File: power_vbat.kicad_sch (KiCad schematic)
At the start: 8 parts, among them J3 ESC pads (CURR TX M4 M3 M2 M1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

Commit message: updoot
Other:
- note added: "BOARD INPUTS: regulated 5 V at J3 pin 7 from an external converter, plus USB VBUS at J4. External choices: 2S-6S -> 5 V / 3 A buck, or 1S 18650 -> 5 V boost. J3 pin 9 carries raw battery voltage only to the R27/R28 sense divider. 5V_IN supplies servo power (J7 rows 7-10) and Q1. GPS/ELRS use V3V3_SYS."
- note added: "ESC PAD ROW J3: CURR, TX, M4, M3, M2, M1, 5V_IN, GND, VBAT. CURR -> R53/C78 -> GPIO42 (ADC2); TX -> R54 -> GPIO32 (PIO UART RX). Motor PWM4/3/2/1 -> GPIO36/38/39/43. Pin 7 receives regulated 5 V from an external buck or boost; C19 is its bulk capacitor. Pin 9 senses raw battery through R27/R28/C48 to GPIO41 (ADC1); it powers no load. Pad pitch is assumed 2.00 mm: confirm against the physical ESC.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"
- note removed: "BOARD INPUTS: REGULATED 5 V FROM AN EXTERNAL BEC on the ESC pad row J3 pin 7 (5V_IN), and USB VBUS ~5 V (J4). There is no on-board pack buck any more (DESIGN_SPEC "Decisions", 2026-09-17): raw pack reaches this board only as the J3 pin 9 SENSE wire VBAT, which drives the R27/R28/C48 divider and nothing else - no load, no bulk, no copper zone. 5V_IN is the servo / GPS / ELRS bus (IO block rows 1-4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"
- note removed: "ESC PAD ROW J3 (MicoAir AM32 4-in-1 ESC, FC-connection row), NINE PADS. Pads 1-6 are the ESC silkscreen read left to right; pads 7-9 are this board's power entry, added when the on-board pack buck was removed: 1 CURR - analog current sense from the ESC, 12.75 mV/A, 0-3.3 V -> R53/C78 -> GPIO42 (ADC2) on BOARD 1. 2 TX - KISS ESC telemetry, 3.3 V, 115200 baud, ESC output only -> R54 -> GPIO32 (PIO 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"

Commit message: update
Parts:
- C48: value 100n / 16 V X7R, ADC1 -> 100n / 16 V X7R, ADC2
- C78: value 100n / 16 V X7R, ADC2 filter -> 100n / 16 V X7R, ADC1 filter

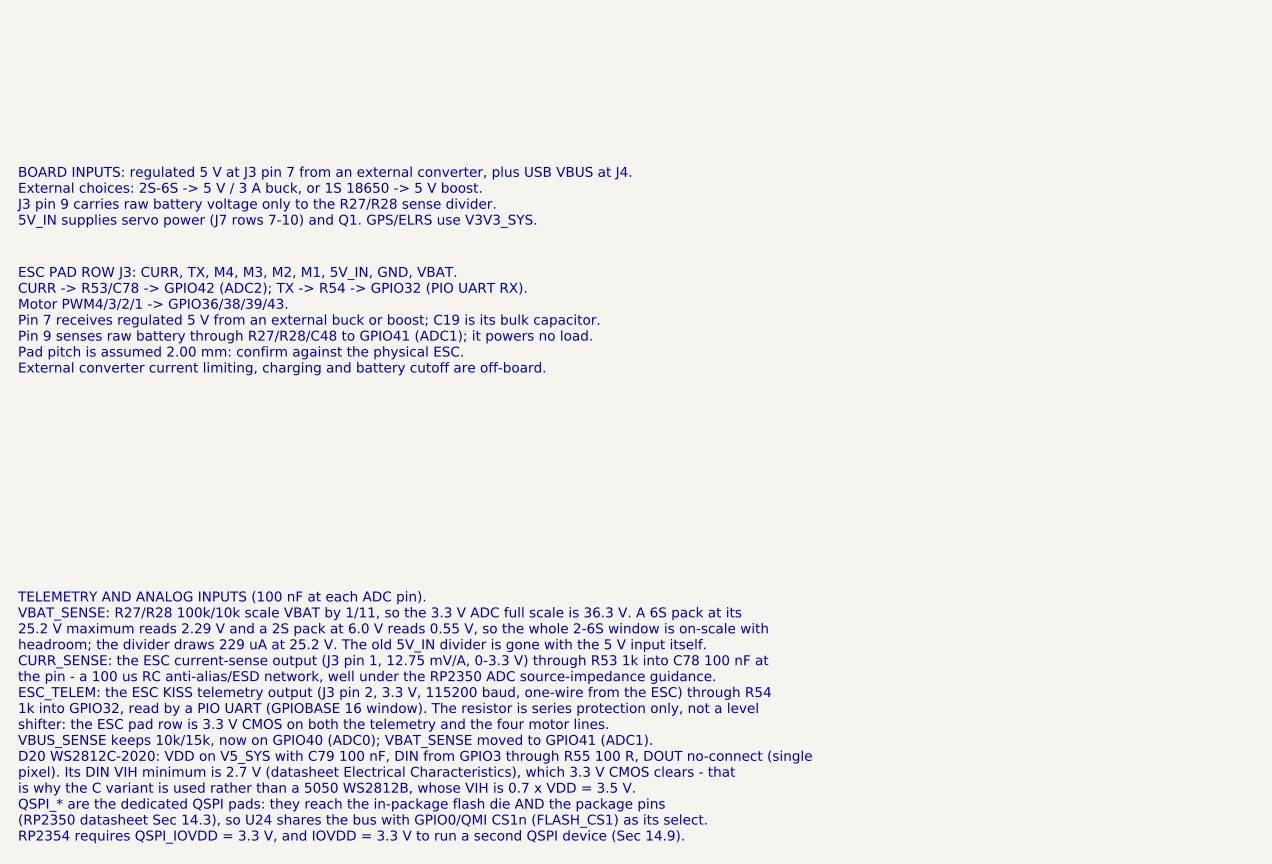
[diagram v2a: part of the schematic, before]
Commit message: finished routing reg, gp under sd & flash, icm solder mask exclusion
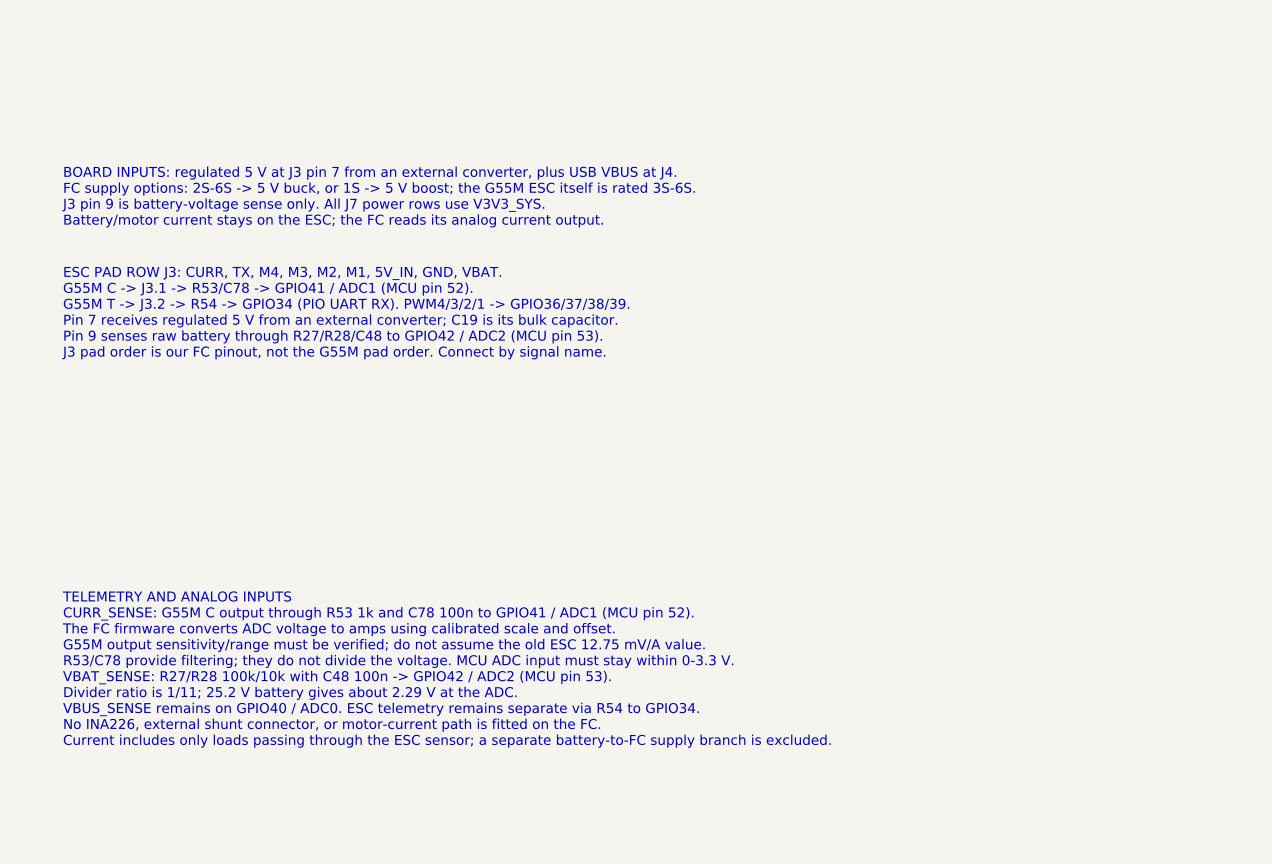
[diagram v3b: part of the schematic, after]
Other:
- note added: "BOARD INPUTS: regulated 5 V at J3 pin 7 from an external converter, plus USB VBUS at J4. FC supply options: 2S-6S -> 5 V buck, or 1S -> 5 V boost; the G55M ESC itself is rated 3S-6S. J3 pin 9 is battery-voltage sense only. All J7 power rows use V3V3_SYS. Battery/motor current stays on the ESC; the FC reads its analog current output."
- note added: "ESC PAD ROW J3: CURR, TX, M4, M3, M2, M1, 5V_IN, GND, VBAT. G55M C -> J3.1 -> R53/C78 -> GPIO41 / ADC1 (MCU pin 52). G55M T -> J3.2 -> R54 -> GPIO34 (PIO UART RX). PWM4/3/2/1 -> GPIO36/37/38/39. Pin 7 receives regulated 5 V from an external converter; C19 is its bulk capacitor. Pin 9 senses raw battery through R27/R28/C48 to GPIO42 / ADC2 (MCU pin 53). J3 pad order is our FC pinout, not the G55M 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"
- note added: "TELEMETRY AND ANALOG INPUTS CURR_SENSE: G55M C output through R53 1k and C78 100n to GPIO41 / ADC1 (MCU pin 52). The FC firmware converts ADC voltage to amps using calibrated scale and offset. G55M output sensitivity/range must be verified; do not assume the old ESC 12.75 mV/A value. R53/C78 provide filtering; they do not divide the voltage. MCU ADC input must stay within 0-3.3 V. VBAT_SENSE: R27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"
- note removed: "BOARD INPUTS: regulated 5 V at J3 pin 7 from an external converter, plus USB VBUS at J4. External choices: 2S-6S -> 5 V / 3 A buck, or 1S 18650 -> 5 V boost. J3 pin 9 carries raw battery voltage only to the R27/R28 sense divider. 5V_IN supplies servo power (J7 rows 7-10) and Q1. GPS/ELRS use V3V3_SYS."
- note removed: "ESC PAD ROW J3: CURR, TX, M4, M3, M2, M1, 5V_IN, GND, VBAT. CURR -> R53/C78 -> GPIO42 (ADC2); TX -> R54 -> GPIO32 (PIO UART RX). Motor PWM4/3/2/1 -> GPIO36/38/39/43. Pin 7 receives regulated 5 V from an external buck or boost; C19 is its bulk capacitor. Pin 9 senses raw battery through R27/R28/C48 to GPIO41 (ADC1); it powers no load. Pad pitch is assumed 2.00 mm: confirm against the physical ESC.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"
- note removed: "TELEMETRY AND ANALOG INPUTS (100 nF at each ADC pin). VBAT_SENSE: R27/R28 100k/10k scale VBAT by 1/11, so the 3.3 V ADC full scale is 36.3 V. A 6S pack at its 25.2 V maximum reads 2.29 V and a 2S pack at 6.0 V reads 0.55 V, so the whole 2-6S window is on-scale with headroom; the divider draws 229 uA at 25.2 V. The old 5V_IN divider is gone with the 5 V input itself. CURR_SENSE: the ESC current-se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"
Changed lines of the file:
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@@
 		(rev "P0 - REVIEW ONLY")
 	)
-	(text "ESC PAD ROW J3: CURR, TX, M4, M3, M2, M1, 5V_IN, GND, VBAT.\nCURR -> R53/C78 -> GPIO42 (ADC2); TX -> R54 -> GPIO32 (PIO UART RX).\nMotor PWM4/3/2/1 -> GPIO36/38/39/43.\nPin 7 receives regulated 5 V from an external buck or boost; C19 is its bulk capacitor.\nPin 9 senses raw battery through R27/R28/C48 to GPIO41 (ADC1); it powers no load.\nPad pitch is assumed 2.00 mm: confirm against the physical ESC.\nExternal converter current limiting, charging and battery cutoff are off-board."
+	(text "ESC PAD ROW J3: CURR, TX, M4, M3, M2, M1, 5V_IN, GND, VBAT.\nG55M C -> J3.1 -> R53/C78 -> GPIO41 / ADC1 (MCU pin 52).\nG55M T -> J3.2 -> R54 -> GPIO34 (PIO UART RX). PWM4/3/2/1 -> GPIO36/37/38/39.\nPin 7 receives regulated 5 V from an external converter; C19 is its bulk capacitor.\nPin 9 senses raw battery through R27/R28/C48 to GPIO42 / ADC2 (MCU pin 53).\nJ3 pad order is our FC pinout, not the G55M pad order. Connect by signal name."
 		(exclude_from_sim no)
-		(at 10 189.115 0)
+		(at 15 189.115 0)
 		(effects
 			(font
@@
 		)
 	)
-	(text "BOARD INPUTS: regulated 5 V at J3 pin 7 from an external converter, plus USB VBUS at J4.\nExternal choices: 2S-6S -> 5 V / 3 A buck, or 1S 18650 -> 5 V boost.\nJ3 pin 9 carries raw battery voltage only to the R27/R28 sense divider.\n5V_IN supplies servo power (J7 rows 7-10) and Q1. GPS/ELRS use V3V3_SYS."
+	(text "BOARD INPUTS: regulated 5 V at J3 pin 7 from an external converter, plus USB VBUS at J4.\nFC supply options: 2S-6S -> 5 V buck, or 1S -> 5 V boost; the G55M ESC itself is rated 3S-6S.\nJ3 pin 9 is battery-voltage sense only. All J7 power rows use V3V3_SYS.\nBattery/motor current stays on the ESC; the FC reads its analog current output."
 		(exclude_from_sim no)
-		(at 10 178 0)
+		(at 15 178 0)
 		(effects
 			(font
@@
 		)
 	)
-	(text "TELEMETRY AND ANALOG INPUTS (100 nF at each ADC pin).\nVBAT_SENSE: R27/R28 100k/10k scale VBAT by 1/11, so the 3.3 V ADC full scale is 36.3 V. A 6S pack at its\n25.2 V maximum reads 2.29 V and a 2S pack at 6.0 V reads 0.55 V, so the whole 2-6S window is on-scale with\nheadroom; the divider draws 229 uA at 25.2 V. The old 5V_IN divider is gone with the 5 V input itself.\nCURR_SENSE: the ESC current-sense output (J3 pin 1, 12.75 mV/A, 0-3.3 V) through R53 1k into C78 100 nF at\nthe pin - a 100 us RC anti-alias/ESD network, well under the RP2350 ADC source-impedance guidance.\nESC_TELEM: the ESC KISS telemetry output (J3 pin 2, 3.3 V, 115200 baud, one-wire from the ESC) through R54\n1k into GPIO32, read by a PIO UART (GPIOBASE 16 window). The resistor is series protection only, not a level\nshifter: the ESC pad row is 3.3 V CMOS on both the telemetry and the four motor lines.\nVBUS_SENSE keeps 10k/15k, now on GPIO40 (ADC0); VBAT_SENSE moved to GPIO41 (ADC1).\nD20 WS2812C-2020: VDD on V5_SYS with C79 100 nF, DIN from GPIO3 through R55 100 R, DOUT no-connect (single\npixel). Its DIN VIH minimum is 2.7 V (datasheet Electrical Characteristics), which 3.3 V CMOS clears - that\nis why the C variant is used rather than a 5050 WS2812B, whose VIH is 0.7 x VDD = 3.5 V.\nQSPI_* are the dedicated QSPI pads: they reach the in-package flash die AND the package pins\n(RP2350 datasheet Sec 14.3), so U24 shares the bus with GPIO0/QMI CS1n (FLASH_CS1) as its select.\nRP2354 requires QSPI_IOVDD = 3.3 V, and IOVDD = 3.3 V to run a second QSPI device (Sec 14.9)."
+	(text "TELEMETRY AND ANALOG INPUTS\nCURR_SENSE: G55M C output through R53 1k and C78 100n to GPIO41 / ADC1 (MCU pin 52).\nThe FC firmware converts ADC voltage to amps using calibrated scale and offset.\nG55M output sensitivity/range must be verified; do not assume the old ESC 12.75 mV/A value.\nR53/C78 provide filtering; they do not divide the voltage. MCU ADC input must stay within 0-3.3 V.\nVBAT_SENSE: R27/R28 100k/10k with C48 100n -> GPIO42 / ADC2 (MCU pin 53).\nDivider ratio is 1/11; 25.2 V battery gives about 2.29 V at the ADC.\nVBUS_SENSE remains on GPIO40 / ADC0. ESC telemetry remains separate via R54 to GPIO34.\nNo INA226, external shunt connector, or motor-current path is fitted on the FC.\nCurrent includes only loads passing through the ESC sensor; a separate battery-to-FC supply branch is excluded."
 		(exclude_from_sim no)
-		(at 10 225.178 0)
+		(at 15 225.178 0)
 		(effects
 			(font
